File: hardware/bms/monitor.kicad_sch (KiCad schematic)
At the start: 111 parts, among them Q2 Q_PMOS_GSD, Q3 Q_PMOS_GSD, U1 BQ76952

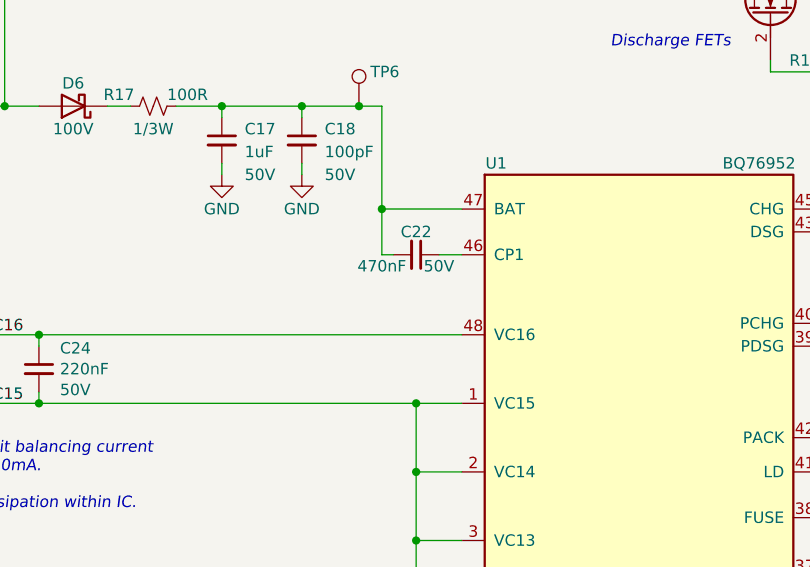
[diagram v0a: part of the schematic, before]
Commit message: Review of BMS board looks good, finished!
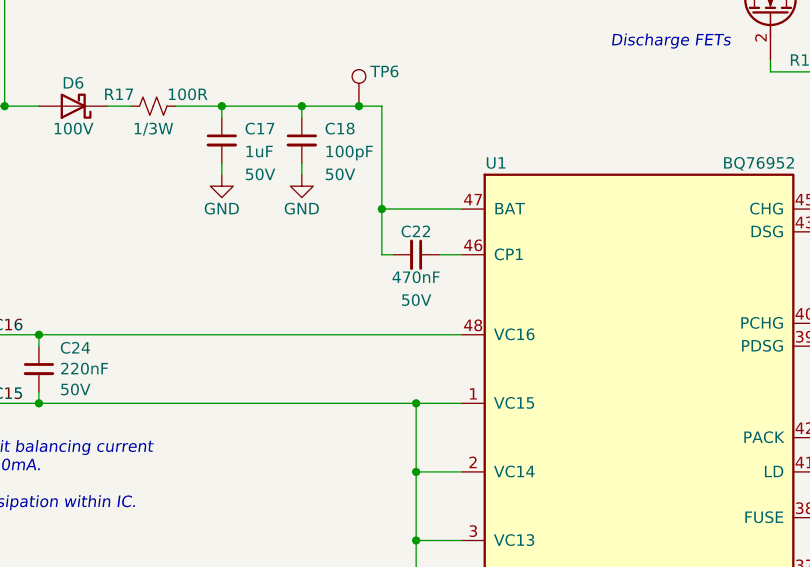
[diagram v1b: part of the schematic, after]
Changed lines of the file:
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@@
       (effects (font (size 1.27 1.27)))
     )
-    (property "Value" "470nF" (at 161.29 92.71 90)
+    (property "Value" "470nF" (at 165.1 93.98 90)
       (effects (font (size 1.27 1.27)))
     )
@@
       (effects (font (size 1.27 1.27)) hide)
     )
-    (property "Voltage" "50V" (at 167.64 92.71 90)
+    (property "Voltage" "50V" (at 165.1 96.52 90)
       (effects (font (size 1.27 1.27)))
     )
